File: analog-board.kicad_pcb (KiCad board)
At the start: 2 copper layers, 200 x 150 mm, 493 parts, among them J1 AC IN, J2 OUT, J3 CONN_20X2, P2 CONN_01X02, Q1 2N3906, Q10 2N3906, Q11 2N3906, Q12 2N3906, Q13 2N3906, Q14 2N3906, Q15 2N3906, Q16 2N3906, Q17 NPN, Q18 NPN, Q19 J111, Q2 2N3906, Q20 2N3906, Q3 2N3906, Q4 2N3906, Q5 2N3906, Q6 BCM857BS, Q7 2N3906, Q8 2N3906, Q9 2N3906, U1 LM13700, U10 ADR01, U11 DG212B, U12 DG212B, U13 DG408, U14 DG408, U15 TL072-, U16 DG408, U17 DG408, U18 LM13700, U19 LM13700, U2 LM13700, U20 74HC75, U21 TL072-, U22 TL074-, U23 TL074-, U24 TL074-, U25 TL074-, U26 TL072-, U27 TL074-, U28 TL074-, U29 LM13700, U3 LM13700, U30 LM13700, U31 TL074-, U32 LM13700, U33 TL074-, U34 TL074-, U35 TL074-, U36 74LV573, U38 0 - 10V, U39 TL074-, U4 DG212B, U40 DG419, U41 0 - 10V, U42 10 - 0V, U43 LM7812, U44 LM7912, U45 DG408, U46 7805, U5 TL074-, U6 AD5556, U7 TL072-, U8 TL074-, U9 AD8672

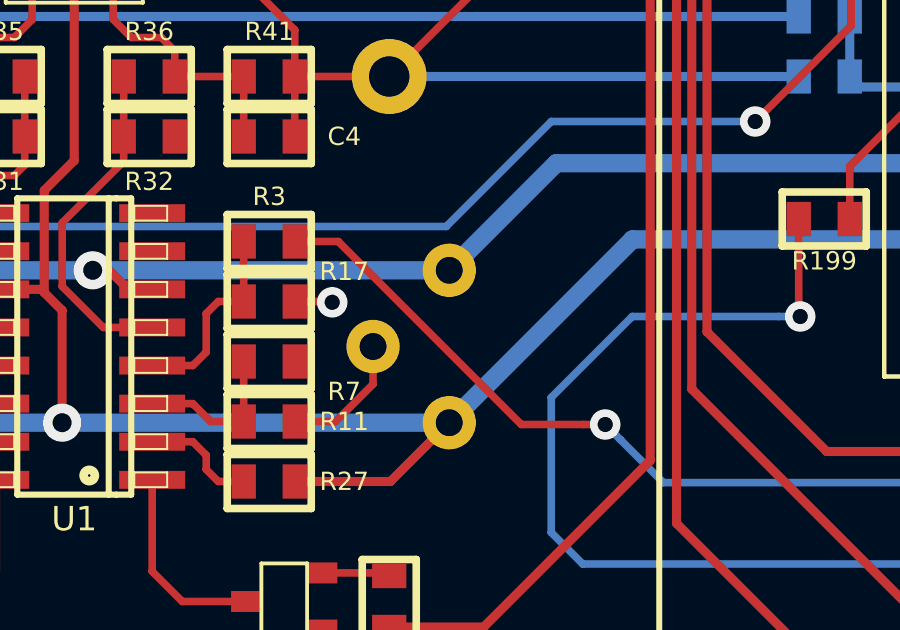
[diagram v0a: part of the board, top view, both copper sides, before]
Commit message: fixed R73 and R78 label swap on PCB silkscreen. Added notes to schematic about changing feedback resistor value to reduce gain of waveform and summing mixers
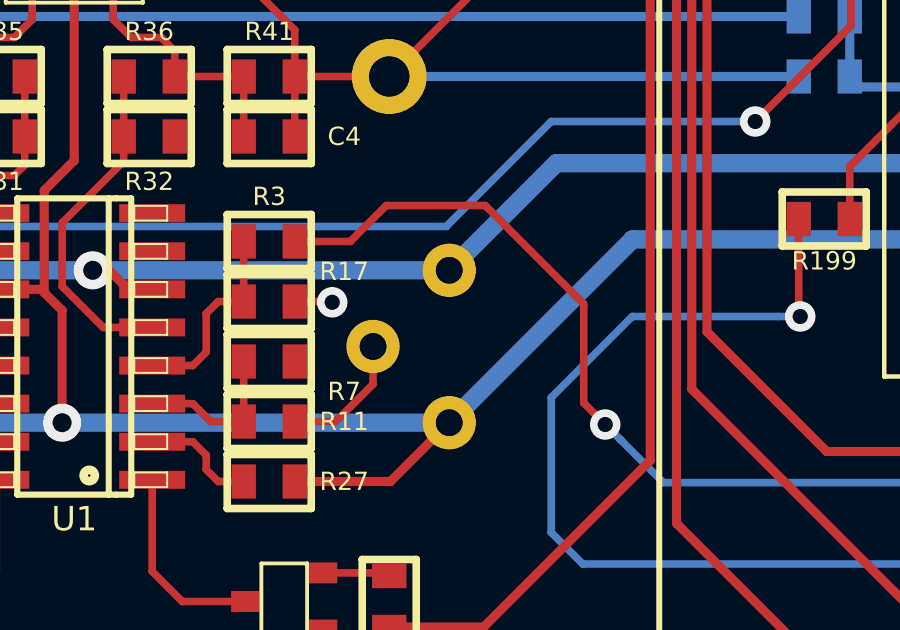
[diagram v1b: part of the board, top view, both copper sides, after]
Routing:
- net EG2: track 262.0 -> 264.9 mm

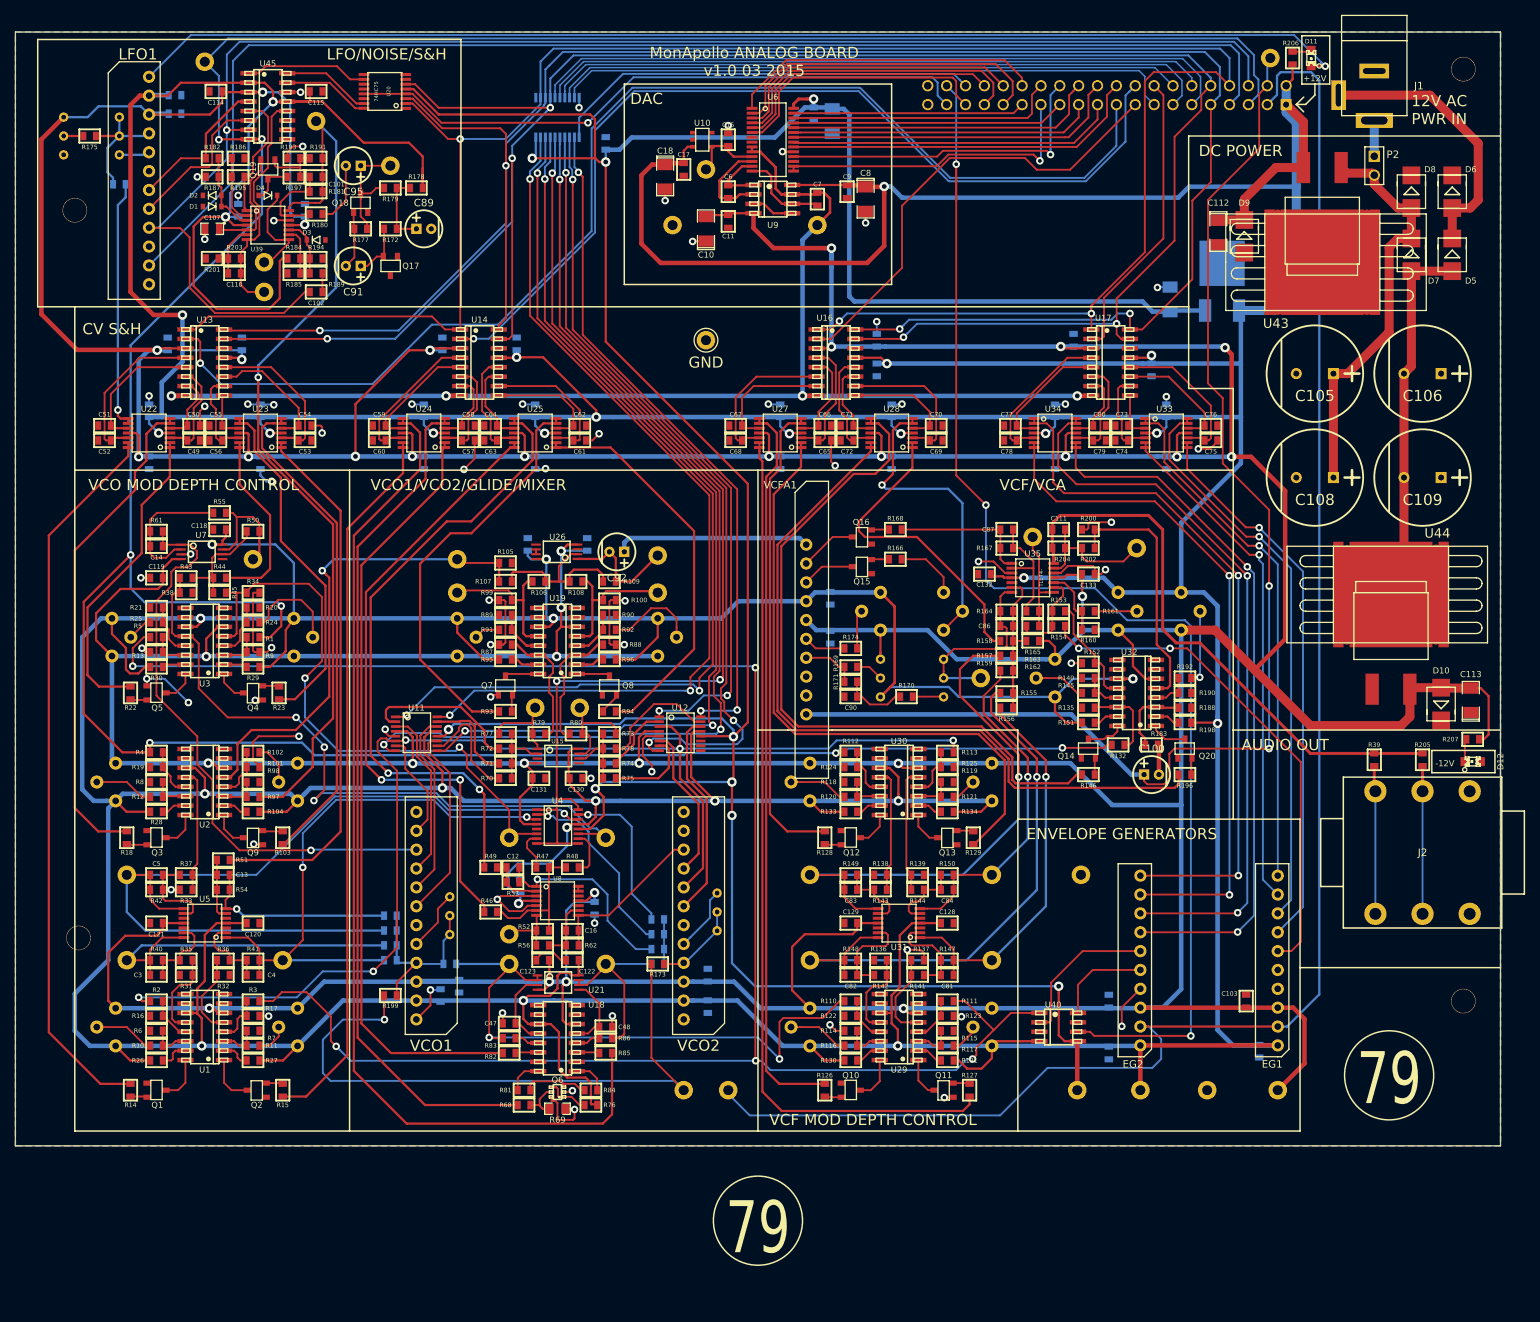
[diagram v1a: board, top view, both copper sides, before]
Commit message: changed C47, C48 and C107 packages to 5mm box/0805 combos
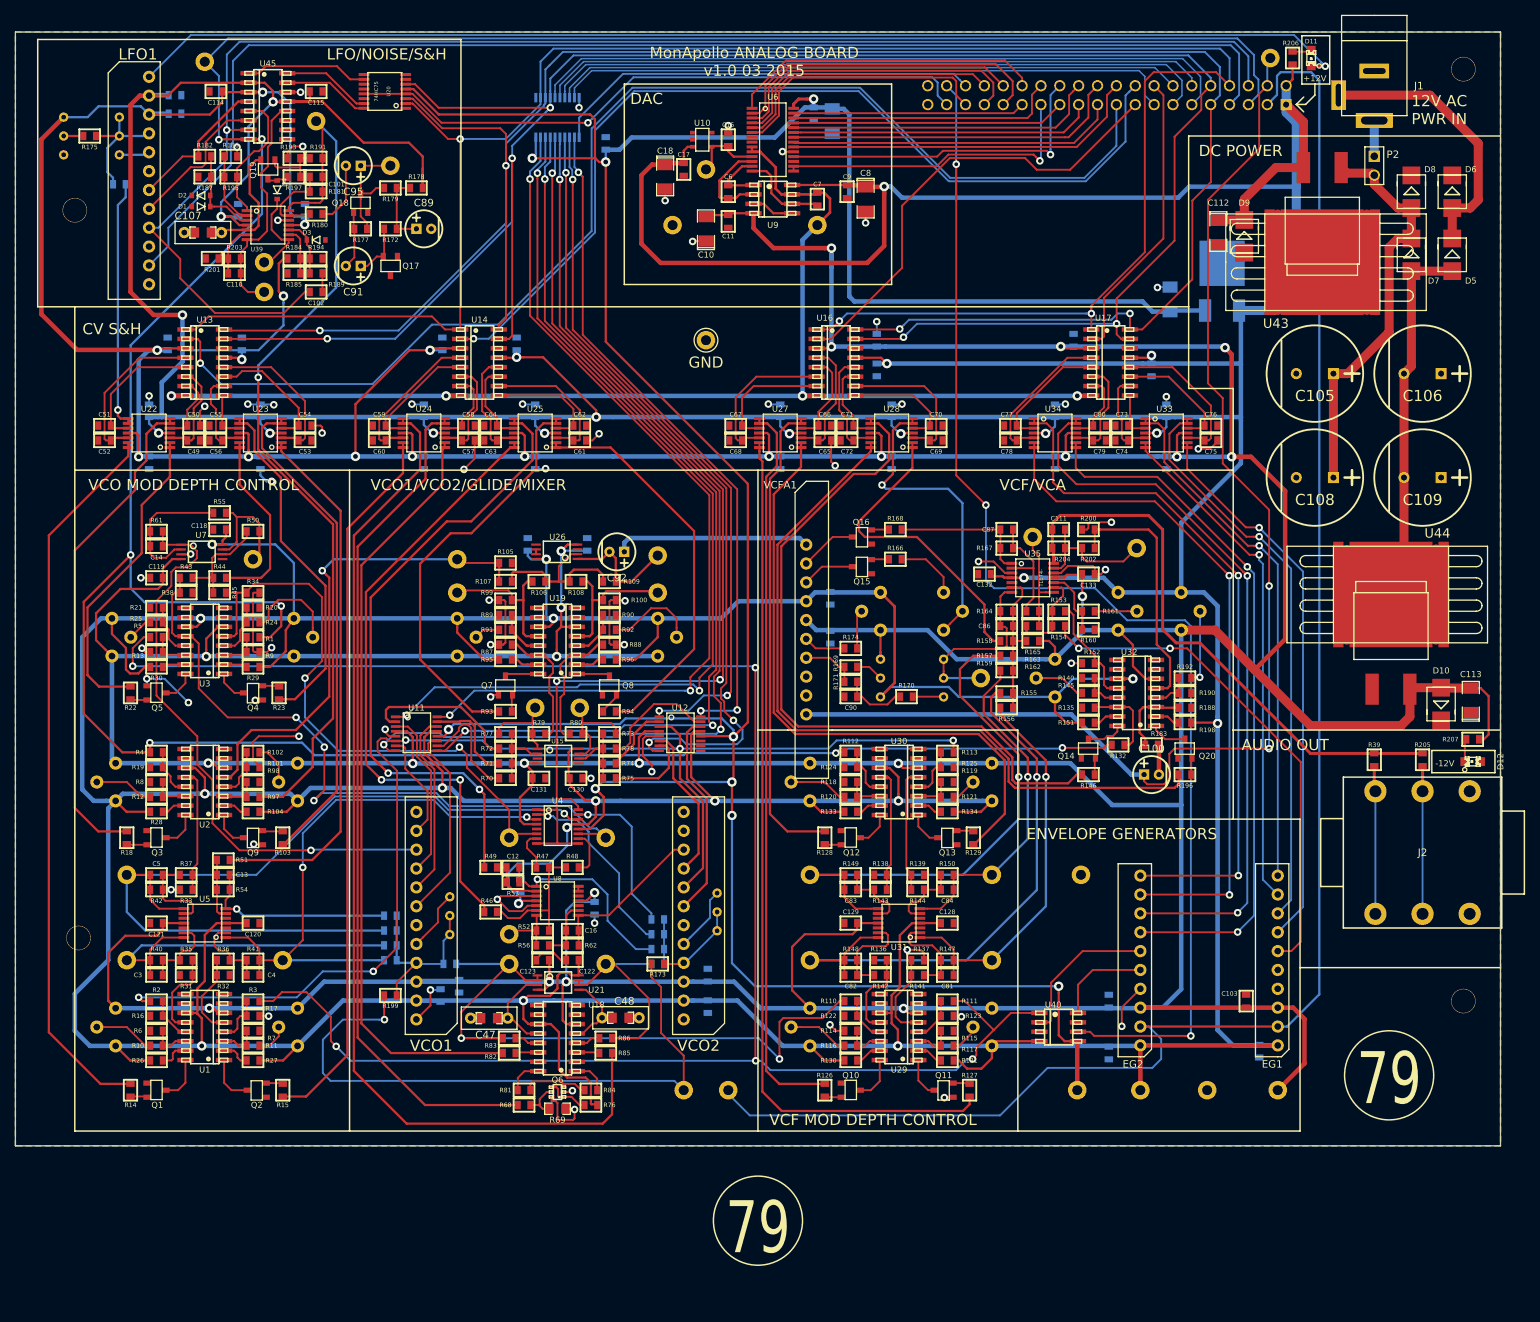
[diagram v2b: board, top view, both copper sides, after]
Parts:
- C107: footprint github-smd:SMD-0805 -> MyModules:CAP-5MM-BOX-0805-COMBO
- C47, C48: footprint MyModules:SM0603-C-JRL -> MyModules:CAP-5MM-BOX-0805-COMBO
- moved C47 2.79 mm to (63.8, 132.8)
- moved C48 2.36 mm to (81.5, 132.8)
- moved D1 1.50 mm to (25.0, 22.0)
- moved D2 1.50 mm to (25.0, 23.5)
- moved D4 1.46 mm to (35.2, 21.2), turned to 270 degrees
- moved C107 1.35 mm to (25.2, 27.0)
- moved R182 1.03 mm to (25.5, 16.8)
- moved R186 1.03 mm to (29.0, 16.8)
- moved R187 1.00 mm to (25.5, 19.5)
- moved R195 1.00 mm to (29.0, 19.5)
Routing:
- net +12V: track 1623.3 -> 1609.3 mm, vias 34 -> 35
- net OSCA GLIDE CV: track 80.6 -> 89.7 mm
- net OSCB GLIDE CV: track 24.1 -> 29.0 mm
- net Net-(D4-Pad1): track 5.83 -> 2.96 mm
- net Net-(C47-Pad1): track 10.9 -> 13.4 mm
- net LFO TUNE: track 206.0 -> 203.5 mm
- net Net-(C107-Pad1): track 15.2 -> 17.1 mm
- net GND: track 370.5 -> 368.8 mm, vias 67 -> 63
- net Net-(D1-Pad1): track 10.9 -> 12.5 mm
- net Net-(D4-Pad2): track 13.6 -> 12.1 mm
- net Net-(C48-Pad1): track 10.1 -> 11.3 mm
- net Net-(R195-Pad1): track 17.4 -> 18.2 mm
- net Net-(LFO1-Pad7): track 20.3 -> 19.5 mm
- net Net-(R186-Pad1): track 9.10 -> 9.76 mm
- net Net-(LFO1-Pad8): track 20.6 -> 20.0 mm

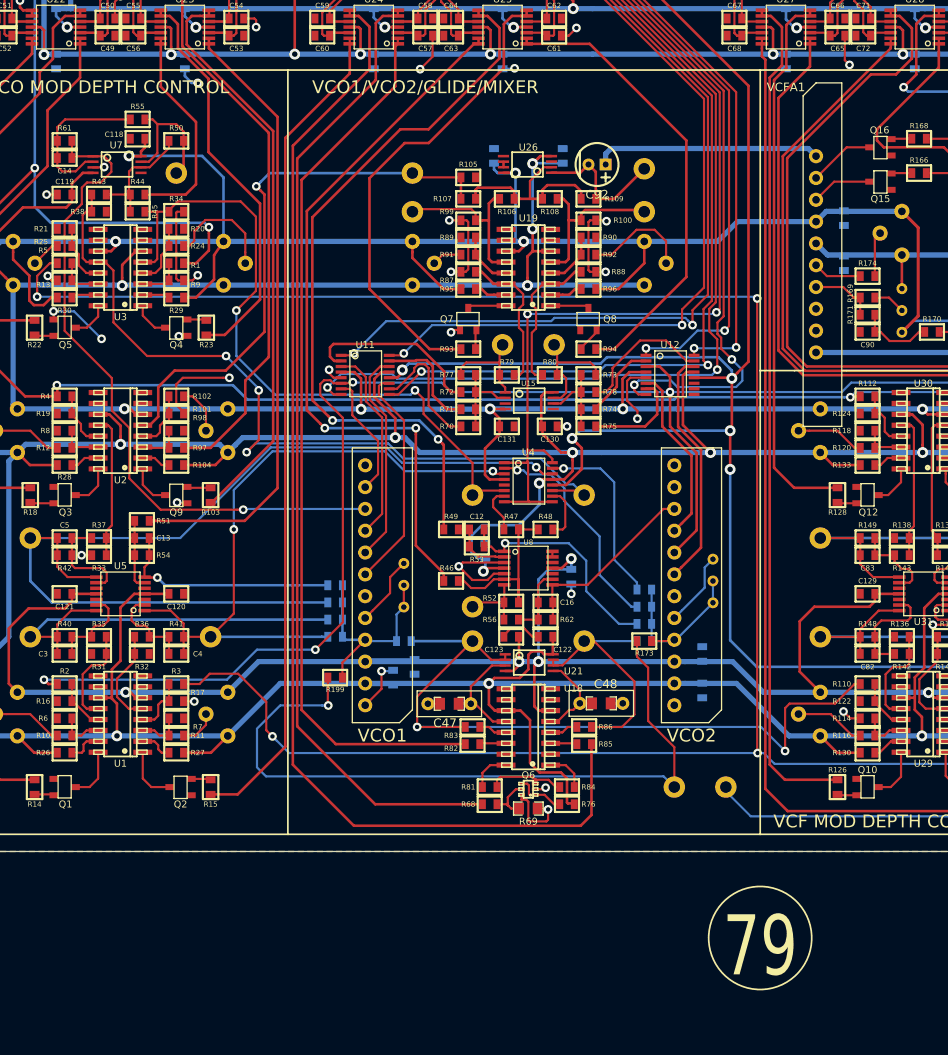
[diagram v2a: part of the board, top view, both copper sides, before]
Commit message: add 220K resistors to PWM LFO modulation summer to balance LFO waveform around 0V
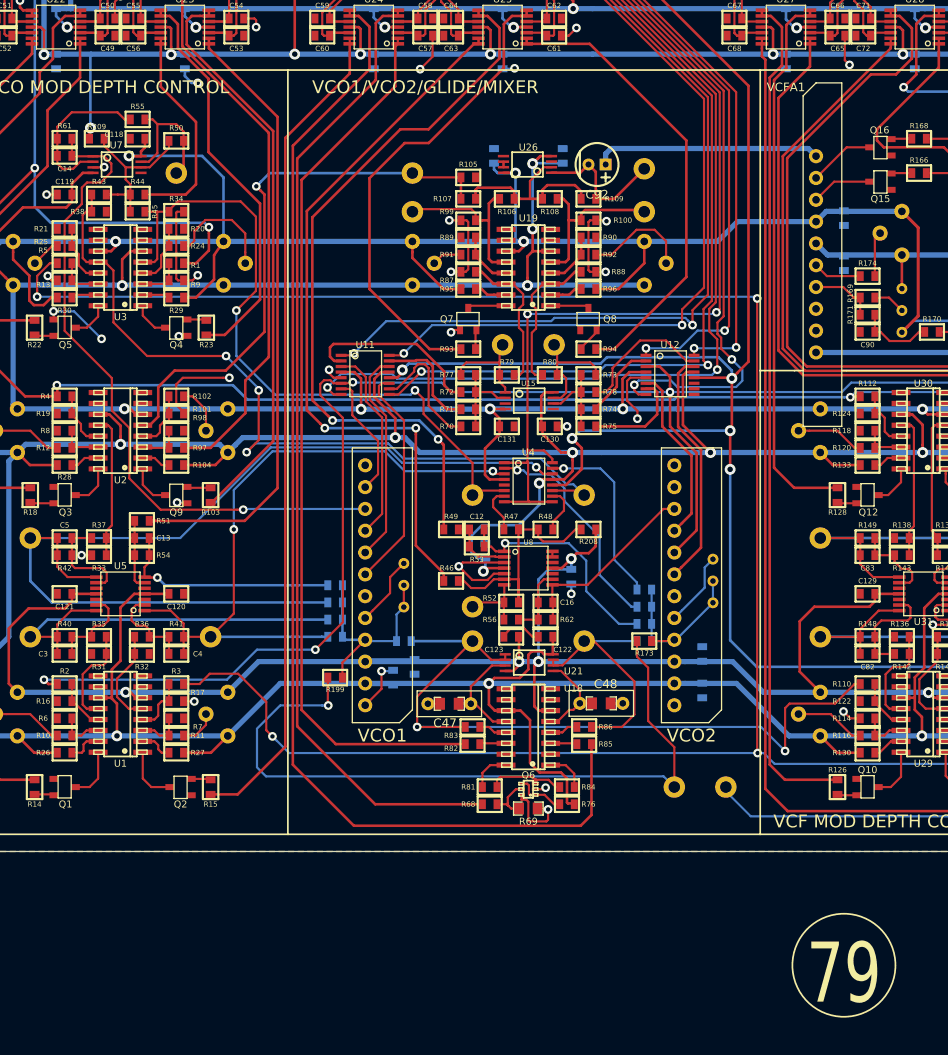
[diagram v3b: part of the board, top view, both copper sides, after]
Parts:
- added R208: 220K, MyModules:SM0603-R-JRL, F.Cu at (80.0, 112.5)
- added R209: 220K, MyModules:SM0603-R-JRL, F.Cu at (22.8, 67.0)
- moved U38 10.3 mm to (109.8, 163.2)
- moved C14 0.25 mm to (19.0, 69.0)
- moved R61 0.25 mm to (19.0, 67.0)
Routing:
- net -12V: track 1267.2 -> 1282.9 mm, vias 33 -> 34
- net Net-(R208-Pad2): track 21.3 -> 27.9 mm
- net Net-(R209-Pad2): track 14.2 -> 19.6 mm
- net Net-(R48-Pad2): track 6.29 -> 5.49 mm
